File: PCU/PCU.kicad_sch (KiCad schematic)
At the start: 12 parts, among them J1 XT60PW-M, J2 B4B-PH-K-S_LF__SN_, J3 B4B-PH-K-S_LF__SN_, J4 Conn_01x03_Pin, J5 Conn_01x03_Pin, J6 Conn_01x03_Pin, J7 Conn_01x03_Pin

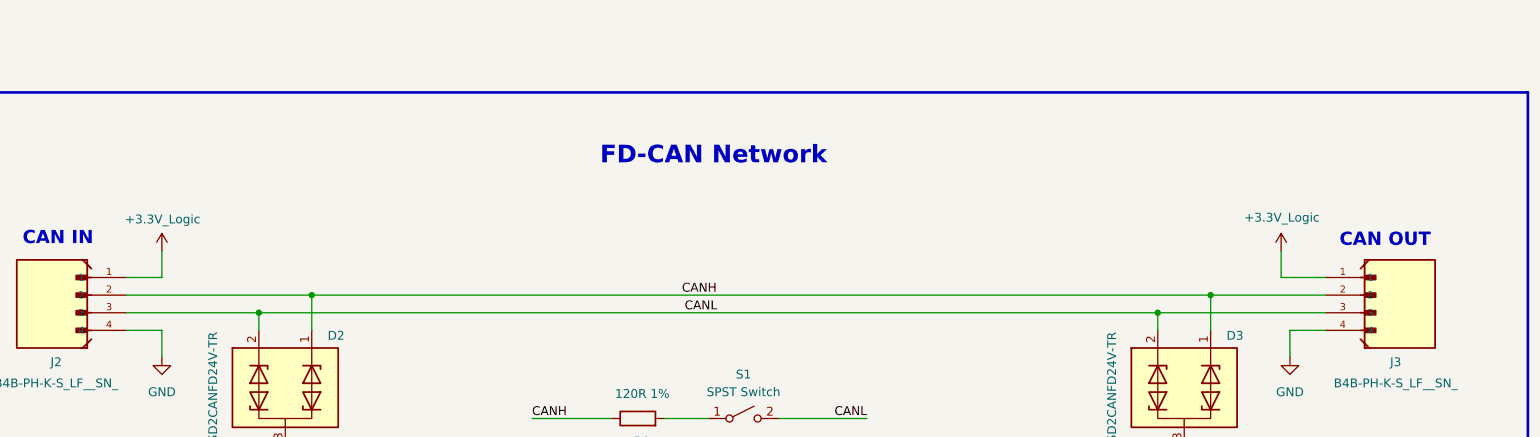
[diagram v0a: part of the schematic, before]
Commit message: PSU Blocks Routed
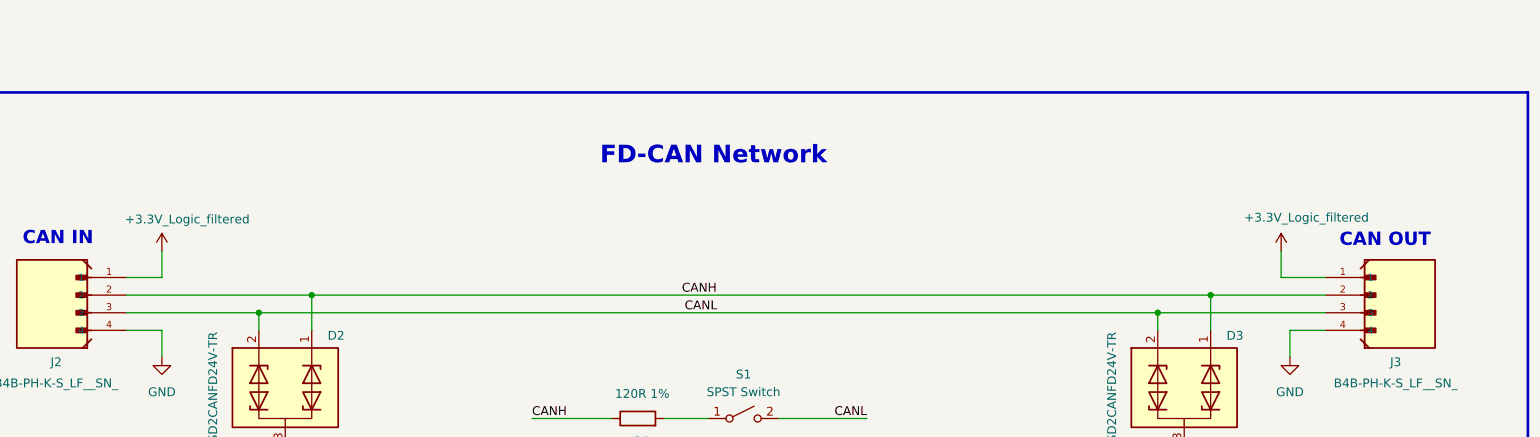
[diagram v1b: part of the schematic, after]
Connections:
- net +3.3V_Logic renamed +3.3V_Logic_filtered
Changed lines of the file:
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@@
 			)
 		)
-		(property "Value" "+3.3V_Logic"
+		(property "Value" "+3.3V_Logic_filtered"
 			(at 65.786 234.188 0)
 			(effects
@@
 			)
 		)
-		(property "Value" "+3.3V_Logic"
+		(property "Value" "+3.3V_Logic_filtered"
 			(at 227.076 233.934 0)
 			(effects

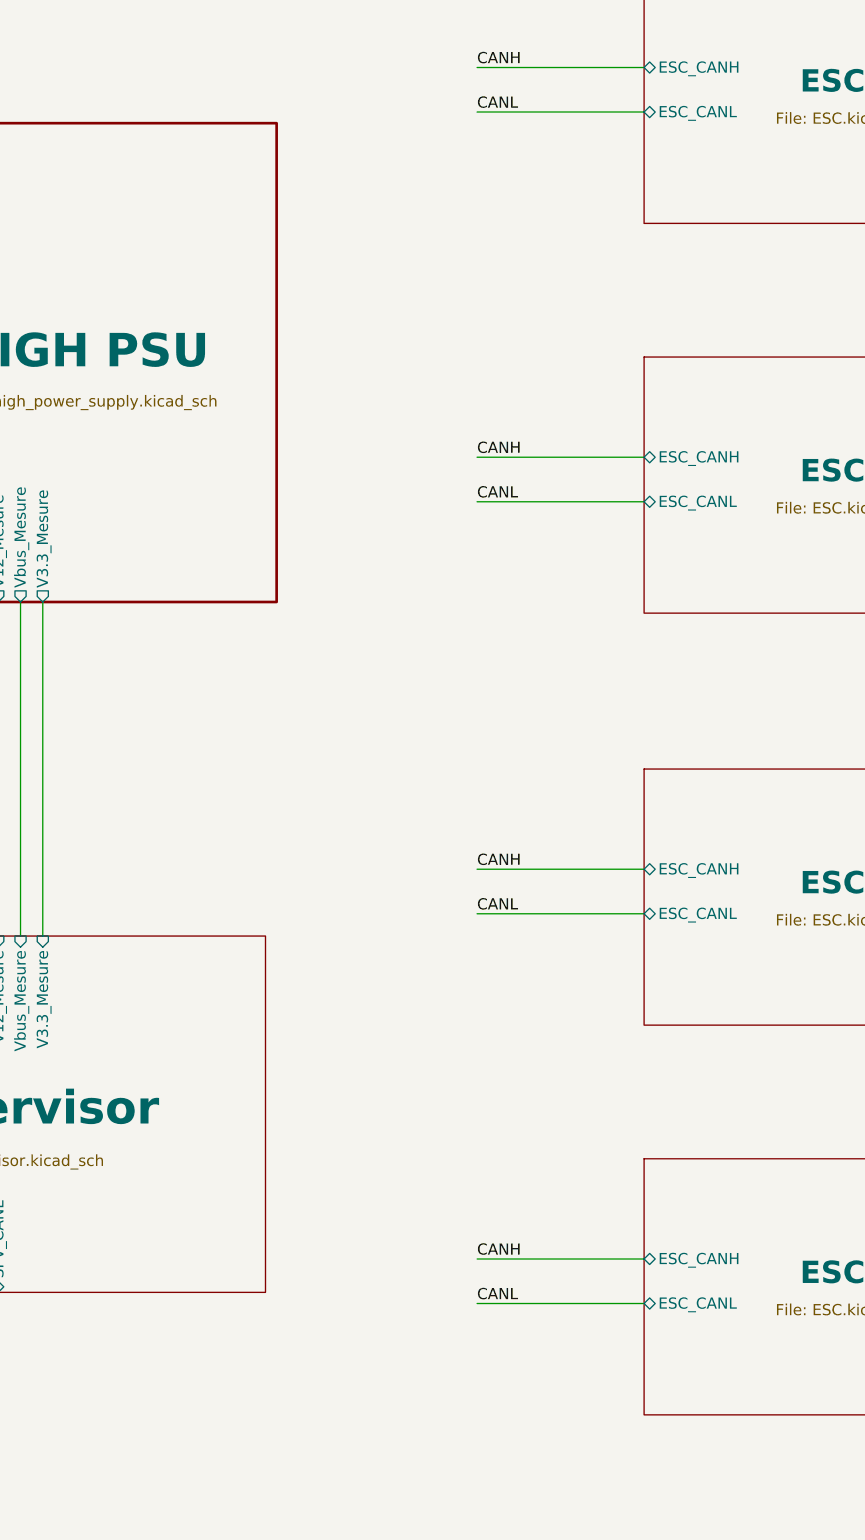
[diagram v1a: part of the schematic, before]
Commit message: ESCs Analog signals routed
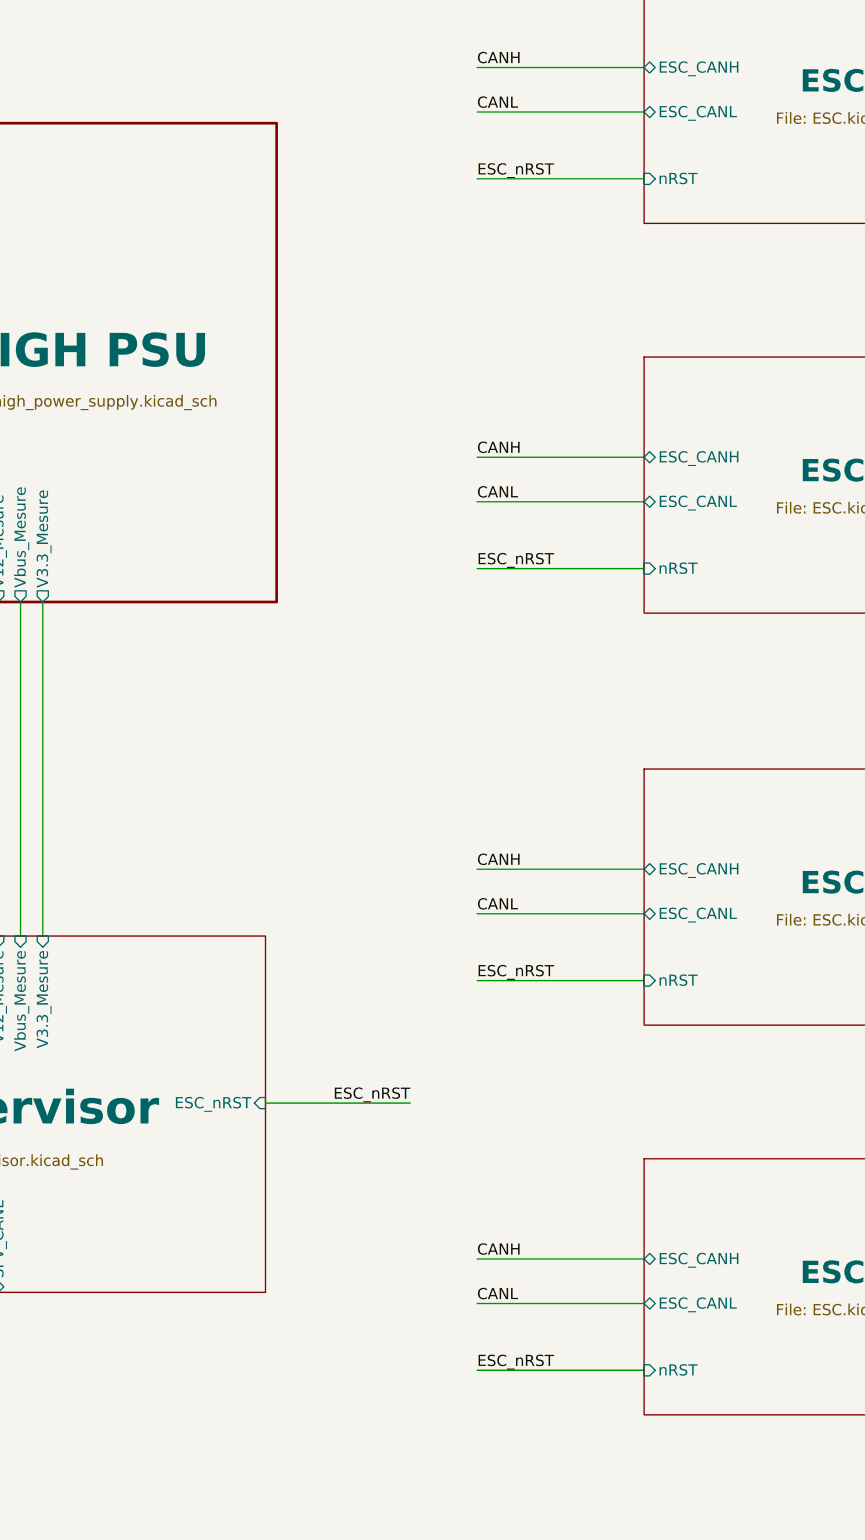
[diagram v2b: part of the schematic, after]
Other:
- sheet ESC_1 ports: added nRST; removed none
- sheet ESC_2 ports: added nRST; removed none
- sheet ESC_3 ports: added nRST; removed none
- sheet ESC_4 ports: added nRST; removed none
- sheet Supervisor ports: added ESC_nRST; removed none
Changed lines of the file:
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@@
 	(wire
 		(pts
+			(xy 302.26 179.07) (xy 321.31 179.07)
+		)
+		(stroke
+			(width 0)
+			(type default)
+		)
+	)
+	(wire
+		(pts
 			(xy 171.45 146.05) (xy 210.82 146.05)
 		)
@@
 	(wire
 		(pts
+			(xy 278.13 148.59) (xy 294.64 148.59)
+		)
+		(stroke
+			(width 0)
+			(type default)
+		)
+	)
+	(wire
+		(pts
 			(xy 53.34 91.44) (xy 53.34 88.9)
 		)
@@
 	(wire
 		(pts
+			(xy 302.26 134.62) (xy 321.31 134.62)
+		)
+		(stroke
+			(width 0)
+			(type default)
+		)
+	)
+	(wire
+		(pts
 			(xy 247.65 170.18) (xy 247.65 182.88)
 		)
@@
 	(wire
 		(pts
+			(xy 302.26 87.63) (xy 321.31 87.63)
+		)
+		(stroke
+			(width 0)
+			(type default)
+		)
+	)
+	(wire
+		(pts
 			(xy 33.02 78.74) (xy 33.02 88.9)
 		)
@@
 	(wire
 		(pts
+			(xy 302.26 43.18) (xy 321.31 43.18)
+		)
+		(stroke
+			(width 0)
+			(type default)
+		)
+	)
+	(wire
+		(pts
 			(xy 92.71 245.11) (xy 222.25 245.11)
 		)
@@
 		)
 	)
+	(label "ESC_nRST"
+		(at 294.64 148.59 180)
+		(effects
+			(font
+				(size 1.27 1.27)
+			)
+			(justify right bottom)
+		)
+	)
+	(label "ESC_nRST"
+		(at 302.26 179.07 0)
+		(effects
+			(font
+				(size 1.27 1.27)
+			)
+			(justify left bottom)
+		)
+	)
 	(label "CANL"
 		(at 302.26 171.45 0)
@@
 		)
 	)
+	(label "ESC_nRST"
+		(at 302.26 87.63 0)
+		(effects
+			(font
+				(size 1.27 1.27)
+			)
+			(justify left bottom)
+		)
+	)
 	(label "CANH"
 		(at 146.05 245.11 0)
@@
 		)
 	)
+	(label "ESC_nRST"
+		(at 302.26 43.18 0)
+		(effects
+			(font
+				(size 1.27 1.27)
+			)
+			(justify left bottom)
+		)
+	)
 	(label "CANL"
 		(at 247.65 182.88 90)
@@
 		)
 	)
+	(label "ESC_nRST"
+		(at 302.26 134.62 0)
+		(effects
+			(font
+				(size 1.27 1.27)
+			)
+			(justify left bottom)
+		)
+	)
 	(label "CANL"
 		(at 302.26 127 0)
@@
 			)
 		)
+		(pin "ESC_nRST" input
+			(at 278.13 148.59 0)
+			(effects
+				(font
+					(size 1.27 1.27)
+				)
+				(justify right)
+			)
+		)
 		(instances
 			(project "PCU"
@@
 			)
 		)
+		(pin "nRST" input
+			(at 321.31 87.63 180)
+			(effects
+				(font
+					(size 1.27 1.27)
+				)
+				(justify left)
+			)
+		)
 		(instances
 			(project "PCU"
@@
 			)
 		)
+		(pin "nRST" input
+			(at 321.31 43.18 180)
+			(effects
+				(font
+					(size 1.27 1.27)
+				)
+				(justify left)
+			)
+		)
 		(instances
 			(project "PCU"
@@
 			)
 		)
+		(pin "nRST" input
+			(at 321.31 179.07 180)
+			(effects
+				(font
+					(size 1.27 1.27)
+				)
+				(justify left)
+			)
+		)
 		(instances
 			(project "PCU"
@@
 			(effects
 				(font
+					(size 1.27 1.27)
+				)
+				(justify left)
+			)
+		)
+		(pin "nRST" input
+			(at 321.31 134.62 180)
+			(effects
+				(font

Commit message: Digital high speed routing started
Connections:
- net CANH renamed CAN+
- net CANL renamed CAN-
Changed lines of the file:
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@@
 		)
 	)
-	(label "CANL"
+	(label "CAN-"
 		(at 172.72 262.89 180)
 		(effects
@@
 		)
 	)
-	(label "CANH"
+	(label "CAN+"
 		(at 302.26 166.37 0)
 		(effects
@@
 		)
 	)
-	(label "CANL"
+	(label "CAN-"
 		(at 302.26 171.45 0)
 		(effects
@@
 		)
 	)
-	(label "CANL"
+	(label "CAN-"
 		(at 302.26 35.56 0)
 		(effects
@@
 		)
 	)
-	(label "CANH"
+	(label "CAN+"
 		(at 146.05 245.11 0)
 		(effects
@@
 		)
 	)
-	(label "CANH"
+	(label "CAN+"
 		(at 124.46 262.89 0)
 		(effects
@@
 		)
 	)
-	(label "CANL"
+	(label "CAN-"
 		(at 247.65 182.88 90)
 		(effects
@@
 		)
 	)
-	(label "CANH"
+	(label "CAN+"
 		(at 302.26 74.93 0)
 		(effects
@@
 		)
 	)
-	(label "CANL"
+	(label "CAN-"
 		(at 302.26 80.01 0)
 		(effects
@@
 		)
 	)
-	(label "CANH"
+	(label "CAN+"
 		(at 302.26 121.92 0)
 		(effects
@@
 		)
 	)
-	(label "CANH"
+	(label "CAN+"
 		(at 302.26 30.48 0)
 		(effects
@@
 		)
 	)
-	(label "CANH"
+	(label "CAN+"
 		(at 243.84 182.88 90)
 		(effects
@@
 		)
 	)
-	(label "CANL"
+	(label "CAN-"
 		(at 302.26 127 0)
 		(effects
@@
 		)
 	)
-	(label "CANL"
+	(label "CAN-"
 		(at 151.13 247.65 180)
 		(effects

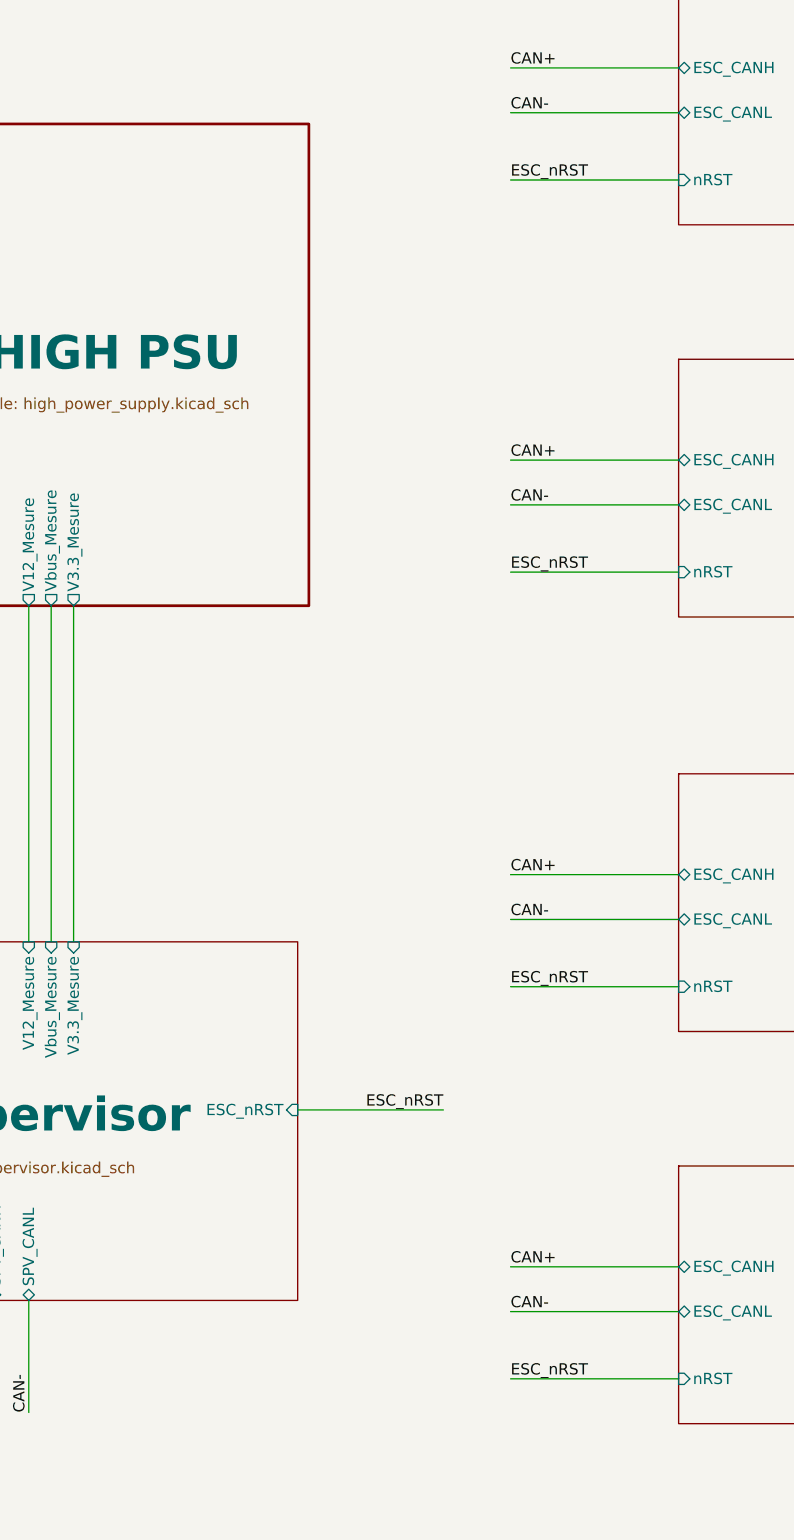
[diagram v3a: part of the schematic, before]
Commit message: Digital signals routed
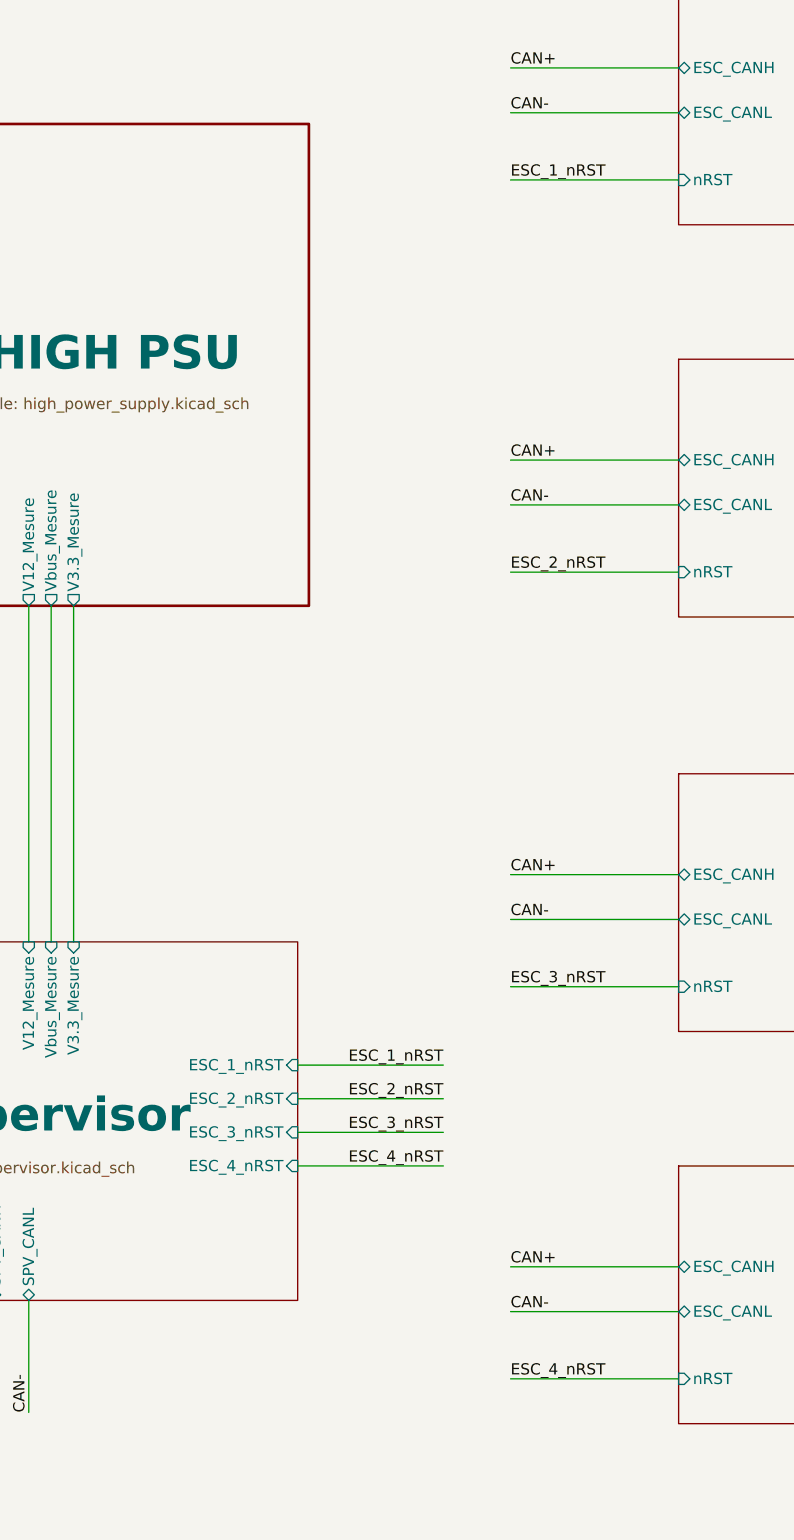
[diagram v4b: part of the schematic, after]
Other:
- sheet Supervisor ports: added ESC_1_nRST, ESC_2_nRST, ESC_3_nRST, ESC_4_nRST; removed ESC_nRST
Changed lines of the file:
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@@
 	(wire
 		(pts
-			(xy 278.13 148.59) (xy 294.64 148.59)
+			(xy 278.13 151.13) (xy 294.64 151.13)
 		)
 		(stroke
@@
 	(wire
 		(pts
+			(xy 278.13 143.51) (xy 294.64 143.51)
+		)
+		(stroke
+			(width 0)
+			(type default)
+		)
+	)
+	(wire
+		(pts
 			(xy 365.76 121.92) (xy 384.81 121.92)
 		)
@@
 	(wire
 		(pts
+			(xy 278.13 154.94) (xy 294.64 154.94)
+		)
+		(stroke
+			(width 0)
+			(type default)
+		)
+	)
+	(wire
+		(pts
 			(xy 365.76 74.93) (xy 384.81 74.93)
 		)
@@
 		(pts
 			(xy 92.71 245.11) (xy 222.25 245.11)
+		)
+		(stroke
+			(width 0)
+			(type default)
+		)
+	)
+	(wire
+		(pts
+			(xy 278.13 147.32) (xy 294.64 147.32)
 		)
 		(stroke
@@
 		)
 	)
+	(label "ESC_2_nRST"
+		(at 294.64 147.32 180)
+		(effects
+			(font
+				(size 1.27 1.27)
+			)
+			(justify right bottom)
+		)
+	)
 	(label "CAN+"
 		(at 302.26 166.37 0)
@@
 		)
 	)
-	(label "ESC_nRST"
-		(at 294.64 148.59 180)
+	(label "ESC_3_nRST"
+		(at 294.64 151.13 180)
 		(effects
 			(font
@@
 		)
 	)
-	(label "ESC_nRST"
+	(label "ESC_4_nRST"
 		(at 302.26 179.07 0)
 		(effects
@@
 		)
 	)
-	(label "ESC_nRST"
+	(label "ESC_2_nRST"
 		(at 302.26 87.63 0)
 		(effects
@@
 		)
 	)
-	(label "ESC_nRST"
+	(label "ESC_1_nRST"
 		(at 302.26 43.18 0)
 		(effects
@@
 			)
 			(justify left bottom)
+		)
+	)
+	(label "ESC_4_nRST"
+		(at 294.64 154.94 180)
+		(effects
+			(font
+				(size 1.27 1.27)
+			)
+			(justify right bottom)
 		)
 	)
@@
 		)
 	)
-	(label "ESC_nRST"
+	(label "ESC_1_nRST"
+		(at 294.64 143.51 180)
+		(effects
+			(font
+				(size 1.27 1.27)
+			)
+			(justify right bottom)
+		)
+	)
+	(label "ESC_3_nRST"
 		(at 302.26 134.62 0)
 		(effects
@@
 			)
 		)
-		(pin "ESC_nRST" input
-			(at 278.13 148.59 0)
-			(effects
-				(font
+		(pin "ESC_3_nRST" input
+			(at 278.13 151.13 0)
+			(effects
+				(font
+					(size 1.27 1.27)
+				)
+				(justify right)
+			)
+		)
+		(pin "ESC_4_nRST" input
+			(at 278.13 154.94 0)
+			(effects
+				(font
+					(size 1.27 1.27)
+				)
+				(justify right)
+			)
+		)
+		(pin "ESC_1_nRST" input
+			(at 278.13 143.51 0)
+			(effects
+				(font
+					(size 1.27 1.27)
+				)
+				(justify right)
+			)
+		)
+		(pin "ESC_2_nRST" input
+			(at 278.13 147.32 0)
+			(effects
+				(font

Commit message: End of Design
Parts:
- added H1, H2: MountingHole_Pad, MountingHole:MountingHole_2.2mm_M2_DIN965_Pad, symbol Mechanical:MountingHole_Pad
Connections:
- net GND: now also H1.1, H2.1

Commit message: Components library added
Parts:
- J1: now not fitted; now left out of the parts list
- J4, J5, J6, J7: now left out of the parts list
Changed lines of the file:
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@@
 		(unit 1)
 		(exclude_from_sim no)
-		(in_bom yes)
+		(in_bom no)
 		(on_board yes)
 		(dnp no)
@@
 		(unit 1)
 		(exclude_from_sim no)
-		(in_bom yes)
+		(in_bom no)
 		(on_board yes)
 		(dnp no)
@@
 		(unit 1)
 		(exclude_from_sim no)
-		(in_bom yes)
+		(in_bom no)
 		(on_board yes)
 		(dnp no)
@@
 		(unit 1)
 		(exclude_from_sim no)
-		(in_bom yes)
-		(on_board yes)
-		(dnp no)
+		(in_bom no)
+		(on_board yes)
+		(dnp yes)
 		(fields_autoplaced yes)
 		(property "Reference" "J1"
@@
 		(unit 1)
 		(exclude_from_sim no)
-		(in_bom yes)
-		(on_board yes)
-		(dnp no)
+		(in_bom no)
+		(on_board yes)
+		(dnp no)

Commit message: Fly controller design started
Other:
- company: BASSINGA Lab -> BASSINGA_LAB
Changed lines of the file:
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@@
 		(date "2025-05-21")
 		(rev "v1.0")
-		(company "BASSINGA Lab")
+		(company "BASSINGA_LAB")
+		(comment 1 "Copyright © 2025 Andresse Brisel BASSINGA ")
 	)
 	(rectangle
